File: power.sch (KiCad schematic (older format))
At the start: 31 parts, among them J24 Power, Q5 2N7002NXAK, Q6 BSH202, Q7 2N7002NXAK, Q8 BSH202, U6 LMR14010ADDCR, U7 LMR14010ADDCR

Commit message: Added images Added information to schematic Added information to layout
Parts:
- renumbered C33 to C29, C34 to C30, C35 to C31, C36 to C32, C37 to C33, C38 to C34, D4 to D2, D5 to D3, D6 to D4, D7 to D5, J24 to J20, R23 to R27, R24 to R28, R36 to R29, R29 to R30, R37 to R31, R30 to R32, R31 to R33, R32 to R34, R33 to R35, R34 to R36, R35 to R37

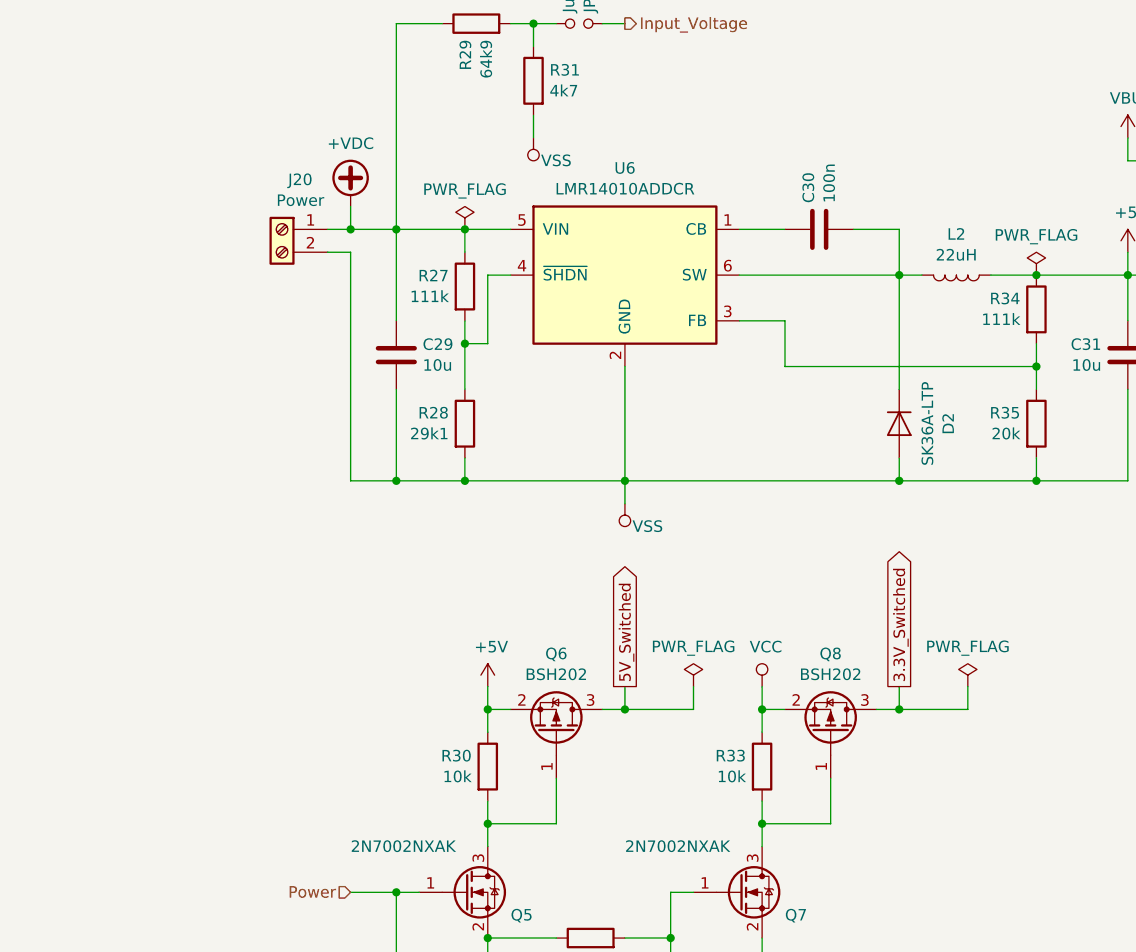
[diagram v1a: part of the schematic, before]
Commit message: Added reverse polarity protection Improved power switch mosfets
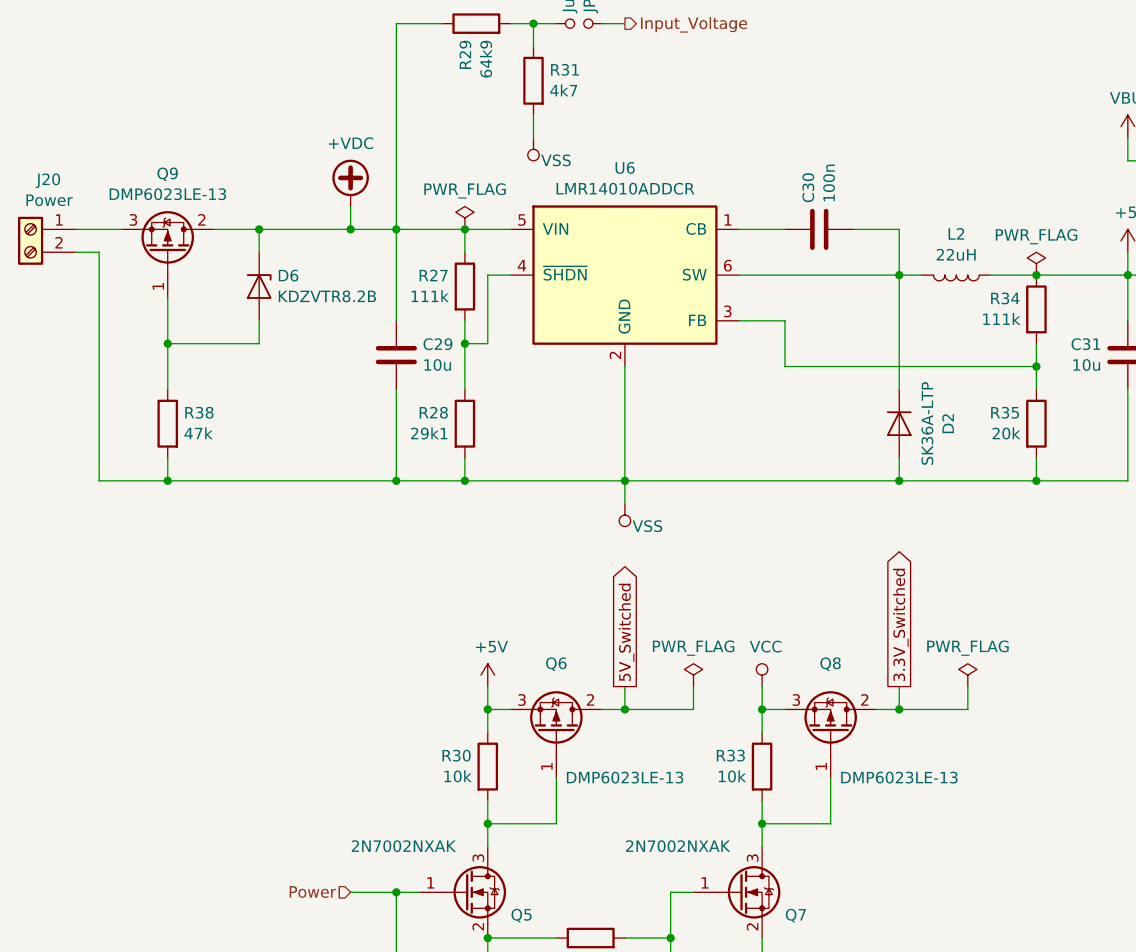
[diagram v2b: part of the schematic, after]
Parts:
- removed Q6, Q8: BSH202, Package_TO_SOT_SMD:SOT-23, symbol Device:Q_PMOS_GSD
- added D6: KDZVTR8.2B, Diode_SMD:D_SOD-123F, symbol Device:D_Zener
- added Q6, Q8, Q9: DMP6023LE-13, Package_TO_SOT_SMD:SOT-223-3_TabPin2, symbol Device:Q_PMOS_GDS
- added R38: 47k, Resistor_SMD:R_0603_1608Metric, symbol Device:R
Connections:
- net +5V: now also Q6.3 (S)
- net +VDC: now also D6.1 (K), Q9.2 (D); no longer J20.1 (Pin_1)
- net 3.3V_Switched: now also Q8.2 (D)
- net 5V_Switched: now also Q6.2 (D)
- net VCC: now also Q8.3 (S)
- net VSS: now also R38.2
- net at Q5.3 (D), R30.2: now also Q6.1 (G)
- net at Q7.3 (D), R33.2: now also Q8.1 (G)
- new net: D6.2 (A), Q9.1 (G), R38.1
- new net: J20.1 (Pin_1), Q9.3 (S)
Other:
- moved on the sheet: J20
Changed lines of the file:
@@
 L Connector:Screw_Terminal_01x02 J20
 U 1 1 5E223786
-P 1700 2100
-F 0 "J20" H 1620 2317 50  0000 C CNN
-F 1 "Power" H 1620 2226 50  0000 C CNN
-F 2 "TerminalBlock:TerminalBlock_bornier-2_P5.08mm" H 1700 2100 50  0001 C CNN
-F 3 "~" H 1700 2100 50  0001 C CNN
-	1    1700 2100
+P 600 2100
+F 0 "J20" H 520 2317 50  0000 C CNN
+F 1 "Power" H 520 2226 50  0000 C CNN
+F 2 "TerminalBlock:TerminalBlock_bornier-2_P5.08mm" H 600 2100 50  0001 C CNN
+F 3 "~" H 600 2100 50  0001 C CNN
+	1    600  2100
 	-1   0    0    -1
 $EndComp
@@
 $EndComp
 Wire Wire Line
-	1900 2100 2000 2100
-Wire Wire Line
 	2000 2100 2000 2000
-Wire Wire Line
-	2000 3200 2000 2200
-Wire Wire Line
-	2000 2200 1900 2200
 $Comp
 L power:VSS #PWR?
@@
 $EndComp
 Connection ~ 2000 2100
-Wire Wire Line
-	2000 3200 2200 3200
 Connection ~ 2200 3200
 $Comp
@@
 Wire Wire Line
 	2600 4600 2600 4700
-$Comp
-L Device:Q_PMOS_GSD Q?
-U 1 1 5E1A7A92
-P 2900 4300
-AR Path="/5DD6D4DA/5DE2F431/5E1A7A92" Ref="Q?"  Part="1"
-AR Path="/5DD6D4DA/5DEBB035/5E1A7A92" Ref="Q?"  Part="1"
-AR Path="/5E1BB661/5E1A7A92" Ref="Q?"  Part="1"
-AR Path="/5E2182CD/5E1A7A92" Ref="Q6"  Part="1"
-F 0 "Q6" V 3243 4300 50  0000 C CNN
-F 1 "BSH202" V 3152 4300 50  0000 C CNN
-F 2 "Package_TO_SOT_SMD:SOT-23" H 3100 4400 50  0001 C CNN
-F 3 "~" H 2900 4300 50  0001 C CNN
-F 4 "BSH202" H 2900 4300 50  0001 C CNN "manf#"
-	1    2900 4300
-	0    1    -1   0
-$EndComp
 Wire Wire Line
 	2600 4200 2600 4300
@@
 Wire Wire Line
 	3800 4600 3800 4700
-$Comp
-L Device:Q_PMOS_GSD Q?
-U 1 1 5E1B5BA3
-P 4100 4300
-AR Path="/5DD6D4DA/5DE2F431/5E1B5BA3" Ref="Q?"  Part="1"
-AR Path="/5DD6D4DA/5DEBB035/5E1B5BA3" Ref="Q?"  Part="1"
-AR Path="/5E1BB661/5E1B5BA3" Ref="Q?"  Part="1"
-AR Path="/5E2182CD/5E1B5BA3" Ref="Q8"  Part="1"
-F 0 "Q8" V 4443 4300 50  0000 C CNN
-F 1 "BSH202" V 4352 4300 50  0000 C CNN
-F 2 "Package_TO_SOT_SMD:SOT-23" H 4300 4400 50  0001 C CNN
-F 3 "~" H 4100 4300 50  0001 C CNN
-F 4 "BSH202" H 4100 4300 50  0001 C CNN "manf#"
-	1    4100 4300
-	0    1    -1   0
-$EndComp
 Wire Wire Line
 	3800 4200 3800 4300
@@
 Wire Wire Line
 	3100 1200 3200 1200
+$Comp
+L Device:Q_PMOS_GDS Q6
+U 1 1 5E1E4C69
+P 2900 4300
+F 0 "Q6" V 3200 4300 50  0000 C CNN
+F 1 "DMP6023LE-13" V 2700 4600 50  0000 C CNN
+F 2 "Package_TO_SOT_SMD:SOT-223-3_TabPin2" H 3100 4400 50  0001 C CNN
+F 3 "~" H 2900 4300 50  0001 C CNN
+	1    2900 4300
+	0    1    -1   0
+$EndComp
+$Comp
+L Device:Q_PMOS_GDS Q8
+U 1 1 5E1F671A
+P 4100 4300
+F 0 "Q8" V 4400 4300 50  0000 C CNN
+F 1 "DMP6023LE-13" V 3900 4600 50  0000 C CNN
+F 2 "Package_TO_SOT_SMD:SOT-223-3_TabPin2" H 4300 4400 50  0001 C CNN
+F 3 "~" H 4100 4300 50  0001 C CNN
+	1    4100 4300
+	0    1    -1   0
+$EndComp
+$Comp
+L Device:Q_PMOS_GDS Q9
+U 1 1 5E209E3F
+P 1200 2200
+F 0 "Q9" V 1543 2200 50  0000 C CNN
+F 1 "DMP6023LE-13" V 1452 2200 50  0000 C CNN
+F 2 "Package_TO_SOT_SMD:SOT-223-3_TabPin2" H 1400 2300 50  0001 C CNN
+F 3 "~" H 1200 2200 50  0001 C CNN
+	1    1200 2200
+	0    1    -1   0
+$EndComp
+Wire Wire Line
+	800  2200 900  2200
+Wire Wire Line
+	900  2200 900  3200
+Wire Wire Line
+	900  3200 1200 3200
+Wire Wire Line
+	1200 3100 1200 3200
+Connection ~ 1200 3200
+Wire Wire Line
+	1200 2800 1200 2600
+Wire Wire Line
+	800  2100 1000 2100
+Wire Wire Line
+	1400 2100 1600 2100
+Wire Wire Line
+	1200 3200 2200 3200
+$Comp
+L Device:D_Zener D6
+U 1 1 5E23D97F
+P 1600 2350
+F 0 "D6" V 1554 2429 50  0000 L CNN
+F 1 "KDZVTR8.2B" V 1645 2429 50  0000 L CNN
+F 2 "Diode_SMD:D_SOD-123F" H 1600 2350 50  0001 C CNN
+F 3 "~" H 1600 2350 50  0001 C CNN
+F 4 "KDZVTR8.2B" V 1600 2350 50  0001 C CNN "manf#"
+	1    1600 2350
+	0    1    1    0
+$EndComp
+Wire Wire Line
+	1600 2100 1600 2200
+Connection ~ 1600 2100
+Wire Wire Line
+	1600 2100 2000 2100
+Wire Wire Line
+	1600 2500 1600 2600
+Wire Wire Line
+	1600 2600 1200 2600
+Connection ~ 1200 2600
+Wire Wire Line
+	1200 2600 1200 2400
+$Comp
+L Device:R R?
+U 1 1 5E25AD93
+P 1200 2950
+AR Path="/5DD6D4DA/5DD6D50E/5E25AD93" Ref="R?"  Part="1"
+AR Path="/5DD6D4DA/5DDED058/5E25AD93" Ref="R?"  Part="1"
+AR Path="/5DD6D4DA/5DDED066/5E25AD93" Ref="R?"  Part="1"
+AR Path="/5DD6D4DA/5DDED074/5E25AD93" Ref="R?"  Part="1"
+AR Path="/5DD6D4DA/5DD6D549/5E25AD93" Ref="R?"  Part="1"
+AR Path="/5DD6D4DA/5DDFF593/5E25AD93" Ref="R?"  Part="1"
+AR Path="/5DD6D4DA/5DE2F431/5E25AD93" Ref="R?"  Part="1"
+AR Path="/5E15DEC3/5E25AD93" Ref="R?"  Part="1"
+AR Path="/5E151517/5E25AD93" Ref="R?"  Part="1"
+AR Path="/5E1C55BA/5E25AD93" Ref="R?"  Part="1"
+AR Path="/5E2182CD/5E25AD93" Ref="R38"  Part="1"
+F 0 "R38" H 1130 2996 50  0000 R CNN
+F 1 "47k" H 1130 2905 50  0000 R CNN
+F 2 "Resistor_SMD:R_0603_1608Metric" V 1130 2950 50  0001 C CNN
+F 3 "~" H 1200 2950 50  0001 C CNN
+	1    1200 2950
+	-1   0    0    -1
+$EndComp
 $EndSCHEMATC

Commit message: Added reverse polarity protection Changed power switch MOSFETs to a lower RDS(on) model Improved buck converter layout Improved USB layout
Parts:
- R30, R33: value 10k -> 100k
- R38: value 47k -> 1M
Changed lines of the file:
@@
 AR Path="/5E2182CD/5E1A7A89" Ref="R30"  Part="1"
 F 0 "R30" H 2530 4496 50  0000 R CNN
-F 1 "10k" H 2530 4405 50  0000 R CNN
+F 1 "100k" H 2530 4405 50  0000 R CNN
 F 2 "Resistor_SMD:R_0603_1608Metric" V 2530 4450 50  0001 C CNN
 F 3 "~" H 2600 4450 50  0001 C CNN
@@
 AR Path="/5E2182CD/5E1B5B9B" Ref="R33"  Part="1"
 F 0 "R33" H 3730 4496 50  0000 R CNN
-F 1 "10k" H 3730 4405 50  0000 R CNN
+F 1 "100k" H 3730 4405 50  0000 R CNN
 F 2 "Resistor_SMD:R_0603_1608Metric" V 3730 4450 50  0001 C CNN
 F 3 "~" H 3800 4450 50  0001 C CNN
@@
 AR Path="/5E2182CD/5E25AD93" Ref="R38"  Part="1"
 F 0 "R38" H 1130 2996 50  0000 R CNN
-F 1 "47k" H 1130 2905 50  0000 R CNN
+F 1 "1M" H 1130 2905 50  0000 R CNN
 F 2 "Resistor_SMD:R_0603_1608Metric" V 1130 2950 50  0001 C CNN
 F 3 "~" H 1200 2950 50  0001 C CNN

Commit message: Fixed reverse polarity protection
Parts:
- D6: value KDZVTR8.2B -> UDZVTE-1712B; footprint Diode_SMD:D_SOD-123F -> Diode_SMD:D_SOD-323F; manf# KDZVTR8.2B -> UDZVTE-1712B
- Q6, Q8, Q9: manf# (none) -> DMP6023LE-13
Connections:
- net +VDC: now also Q9.3 (S); no longer Q9.2 (D)
- net at J20.1 (Pin_1): now also Q9.2 (D); no longer Q9.3 (S)
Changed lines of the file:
@@
 F 2 "Package_TO_SOT_SMD:SOT-223-3_TabPin2" H 3100 4400 50  0001 C CNN
 F 3 "~" H 2900 4300 50  0001 C CNN
+F 4 "DMP6023LE-13" V 2900 4300 50  0001 C CNN "manf#"
 	1    2900 4300
 	0    1    -1   0
@@
 F 2 "Package_TO_SOT_SMD:SOT-223-3_TabPin2" H 4300 4400 50  0001 C CNN
 F 3 "~" H 4100 4300 50  0001 C CNN
+F 4 "DMP6023LE-13" V 4100 4300 50  0001 C CNN "manf#"
 	1    4100 4300
 	0    1    -1   0
@@
 F 2 "Package_TO_SOT_SMD:SOT-223-3_TabPin2" H 1400 2300 50  0001 C CNN
 F 3 "~" H 1200 2200 50  0001 C CNN
+F 4 "DMP6023LE-13" V 1200 2200 50  0001 C CNN "manf#"
 	1    1200 2200
-	0    1    -1   0
+	0    -1   -1   0
 $EndComp
 Wire Wire Line
@@
 P 1600 2350
 F 0 "D6" V 1554 2429 50  0000 L CNN
-F 1 "KDZVTR8.2B" V 1645 2429 50  0000 L CNN
-F 2 "Diode_SMD:D_SOD-123F" H 1600 2350 50  0001 C CNN
+F 1 "UDZVTE-1712B" V 1645 2429 50  0000 L CNN
+F 2 "Diode_SMD:D_SOD-323F" H 1600 2350 50  0001 C CNN
 F 3 "~" H 1600 2350 50  0001 C CNN
-F 4 "KDZVTR8.2B" V 1600 2350 50  0001 C CNN "manf#"
+F 4 "UDZVTE-1712B" V 1600 2350 50  0001 C CNN "manf#"
 	1    1600 2350
 	0    1    1    0

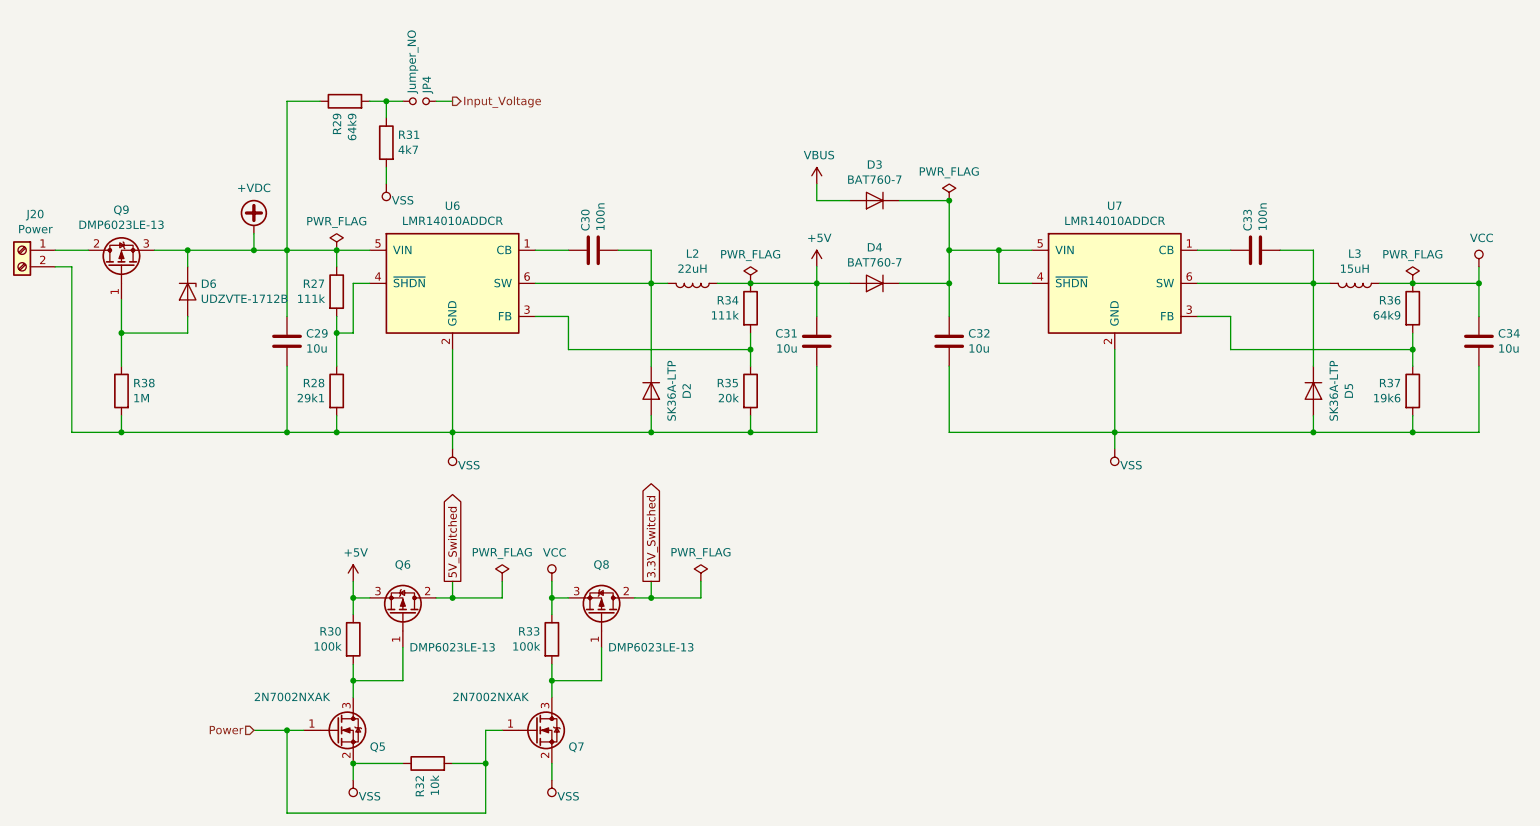
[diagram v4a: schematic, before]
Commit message: Added fuse for USB Added buttons for boot and reset Added version number to PCB Changed several component values for improved manufacturing Added BOM Added component position file
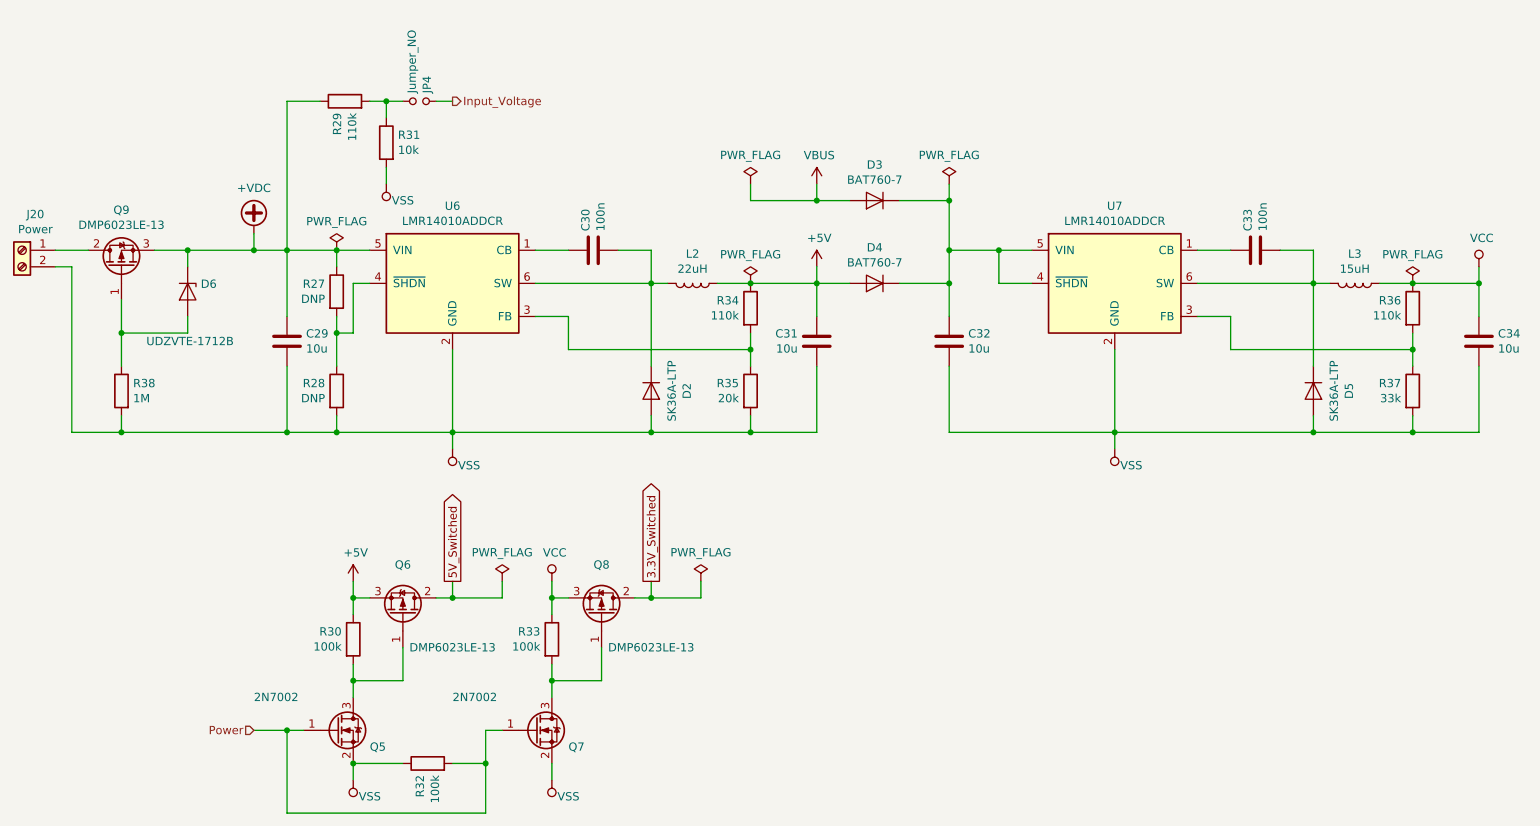
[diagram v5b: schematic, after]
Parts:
- C29, C31, C32, C34: lcsc# (none) -> C13585; manf# CL31B106KBHNNNE -> CL31A106KBHNNNE
- C30, C33: lcsc# (none) -> C14663; manf# CL10B104KB8NNNL -> CC0603KRX7R9BB104
- D2, D5: digikey# (none) -> SK36A-LTPMSCT-ND
- D3, D4: lcsc# (none) -> C124187
- D6: lcsc# (none) -> C84980
- J20: lcsc# (none) -> C8475; manf# (none) -> WJ301V-5.0-2P
- L2: digikey# (none) -> SRN8040-220MCT-ND
- L3: digikey# (none) -> SRN6045-150MCT-ND
- Q5, Q7: value 2N7002NXAK -> 2N7002; lcsc# (none) -> C8545; manf# (none) -> 2N7002
- Q6, Q8, Q9: lcsc# (none) -> C154901
- R27: value 111k -> DNP
- R28: value 29k1 -> DNP
- R29, R36: value 64k9 -> 110k; lcsc# (none) -> C326736; manf# (none) -> RT0603BRD07110KL
- R30, R33: lcsc# (none) -> C25803; manf# (none) -> 0603WAF1003T5E
- R31: value 4k7 -> 10k; lcsc# (none) -> C25804; manf# (none) -> 0603WAF1002T5E
- R32: value 10k -> 100k; lcsc# (none) -> C25803; manf# (none) -> 0603WAF1003T5E
- R34: value 111k -> 110k; lcsc# (none) -> C326736; manf# (none) -> RT0603BRD07110KL
- R35: lcsc# (none) -> C191225; manf# (none) -> ERJPB3B2002V
- R37: value 19k6 -> 33k; lcsc# (none) -> C416700; manf# (none) -> ERJ3RBD3302V
- R38: lcsc# (none) -> C22935; manf# (none) -> 0603WAF1004T5E
- U6, U7: lcsc# (none) -> C388174; manf# (none) -> LMR14010ADDCR
